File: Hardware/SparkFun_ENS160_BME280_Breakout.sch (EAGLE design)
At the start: 37 parts, among them J1 Qwiic Right Angle, J3 Qwiic Right Angle, J4 PTH, U1 AP2127K-1.8V, U2 ENS-160, U3 BME280

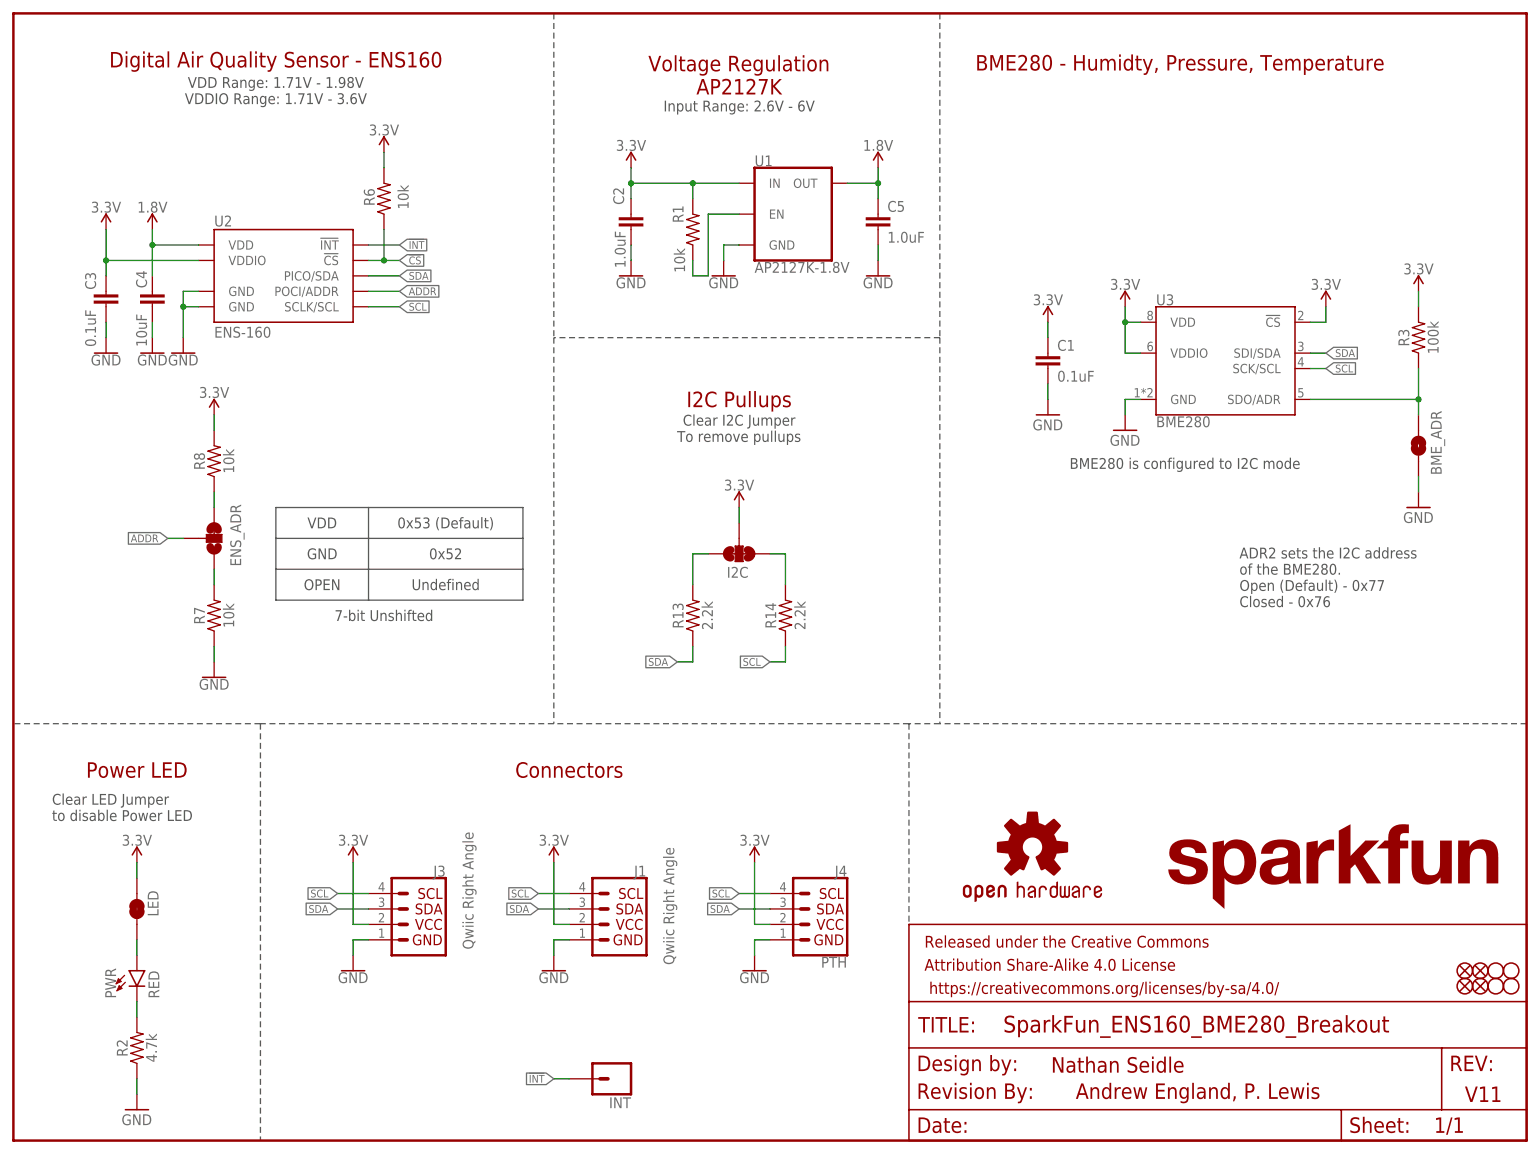
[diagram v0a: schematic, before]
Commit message: added a 100nF cap to VDDIO on BME280
-added C6
-re-routed 3V3 and GND for better return path to GND pads on ICs
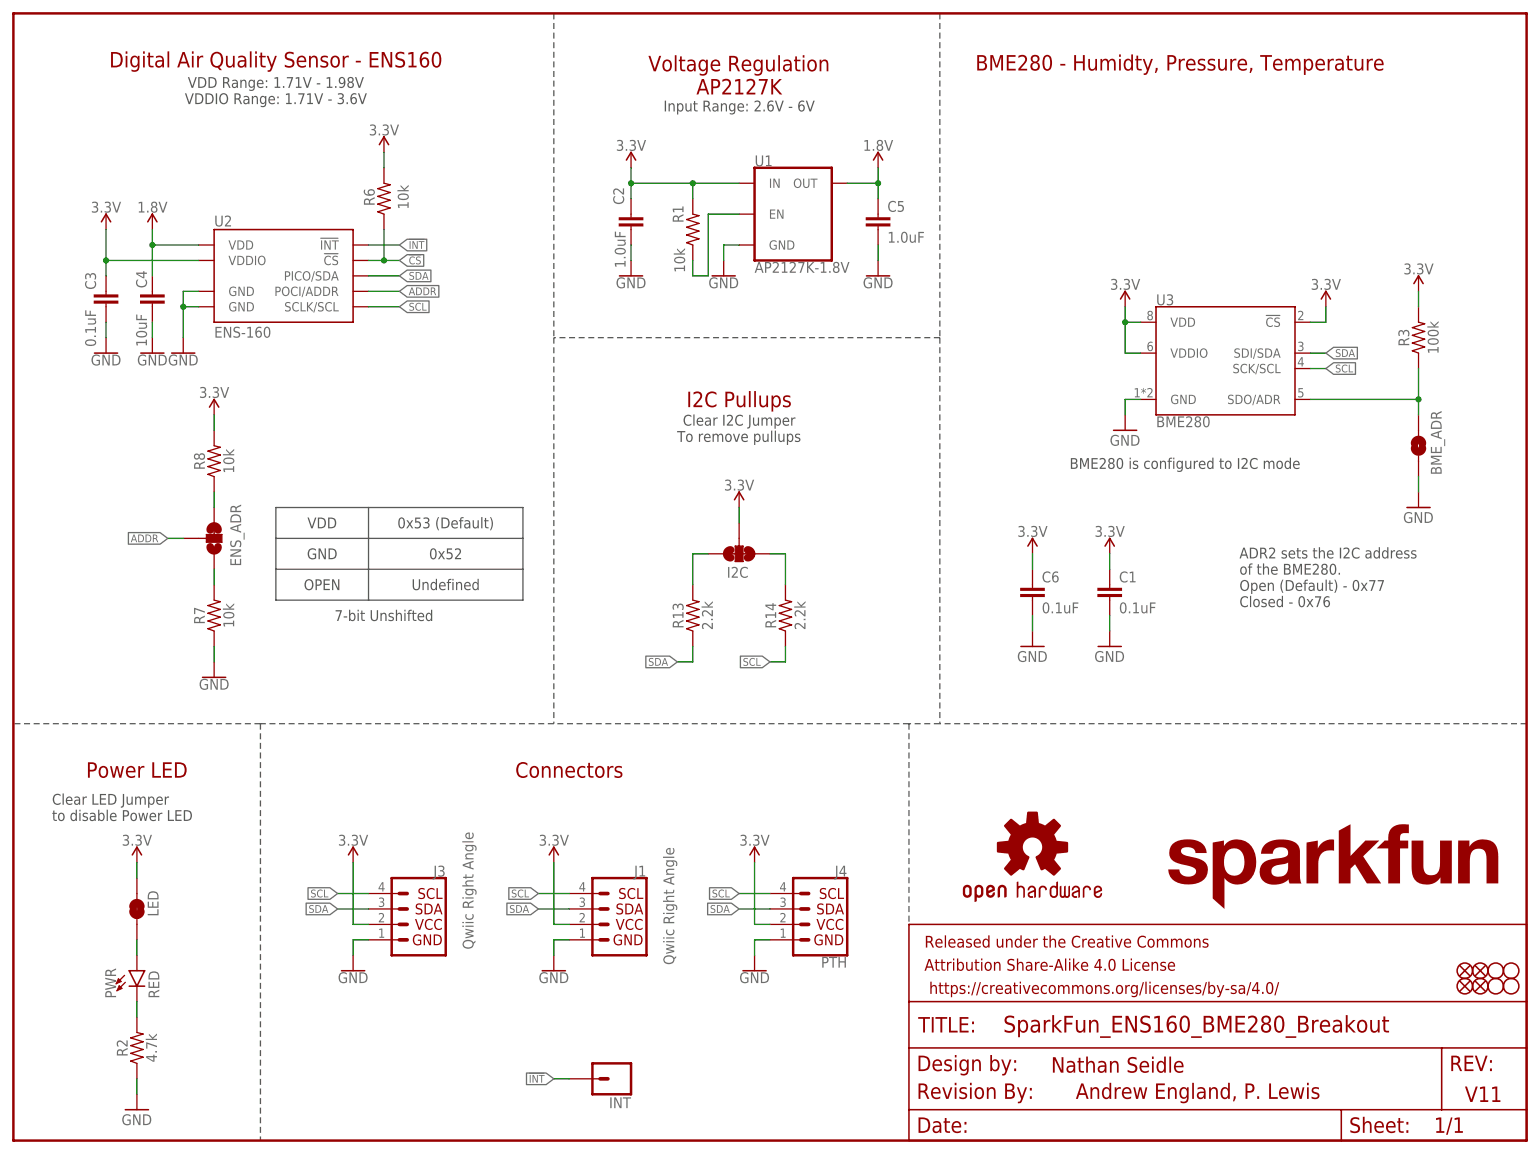
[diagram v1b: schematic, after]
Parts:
- added C6: 0.1uF, SparkFun-Capacitors:0.1UF-0402T-16V-10%
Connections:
- removed net !INT: INT.1
- net !INT!: now also INT.1
- net 3.3V: now also C6.1
- net GND: now also C6.2
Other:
- moved on the sheet: C1
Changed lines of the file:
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@@
 <part name="H1" library="SparkFun-Hardware" deviceset="STAND-OFF" device=""/>
 <part name="H3" library="SparkFun-Hardware" deviceset="STAND-OFF" device=""/>
+<part name="GND13" library="SparkFun-Aesthetics" deviceset="GND" device=""/>
+<part name="C6" library="SparkFun-Capacitors" deviceset="0.1UF" device="-0402T-16V-10%" value="0.1uF"/>
+<part name="SUPPLY13" library="SparkFun-PowerSymbols" deviceset="3.3V" device=""/>
 </parts>
 <sheets>
@@
 <attribute name="VALUE" x="180.34" y="114.3" size="1.778" layer="96" font="vector"/>
 </instance>
-<instance part="GND7" gate="1" x="170.18" y="119.38" smashed="yes">
-<attribute name="VALUE" x="167.64" y="116.84" size="1.778" layer="96" font="vector"/>
-</instance>
-<instance part="C1" gate="G$1" x="170.18" y="127" smashed="yes">
-<attribute name="NAME" x="171.704" y="129.921" size="1.778" layer="95" font="vector"/>
-<attribute name="VALUE" x="171.704" y="124.841" size="1.778" layer="96" font="vector"/>
+<instance part="GND7" gate="1" x="180.34" y="81.28" smashed="yes">
+<attribute name="VALUE" x="177.8" y="78.74" size="1.778" layer="96" font="vector"/>
+</instance>
+<instance part="C1" gate="G$1" x="180.34" y="88.9" smashed="yes">
+<attribute name="NAME" x="181.864" y="91.821" size="1.778" layer="95" font="vector"/>
+<attribute name="VALUE" x="181.864" y="86.741" size="1.778" layer="96" font="vector"/>
 </instance>
 <instance part="GND8" gate="1" x="231.14" y="104.14" smashed="yes">
@@
 <attribute name="VALUE" x="215.9" y="139.954" size="1.778" layer="96" font="vector" align="bottom-center"/>
 </instance>
-<instance part="SUPPLY14" gate="G$1" x="170.18" y="134.62" smashed="yes">
-<attribute name="VALUE" x="170.18" y="137.414" size="1.778" layer="96" font="vector" align="bottom-center"/>
+<instance part="SUPPLY14" gate="G$1" x="180.34" y="96.52" smashed="yes">
+<attribute name="VALUE" x="180.34" y="99.314" size="1.778" layer="96" font="vector" align="bottom-center"/>
 </instance>
 <instance part="U3" gate="U1" x="198.12" y="129.54" smashed="yes">
@@
 <instance part="H1" gate="G$1" x="243.84" y="27.94" smashed="yes"/>
 <instance part="H3" gate="G$1" x="246.38" y="27.94" smashed="yes"/>
+<instance part="GND13" gate="1" x="167.64" y="81.28" smashed="yes">
+<attribute name="VALUE" x="165.1" y="78.74" size="1.778" layer="96" font="vector"/>
+</instance>
+<instance part="C6" gate="G$1" x="167.64" y="88.9" smashed="yes">
+<attribute name="NAME" x="169.164" y="91.821" size="1.778" layer="95" font="vector"/>
+<attribute name="VALUE" x="169.164" y="86.741" size="1.778" layer="96" font="vector"/>
+</instance>
+<instance part="SUPPLY13" gate="G$1" x="167.64" y="96.52" smashed="yes">
+<attribute name="VALUE" x="167.64" y="99.314" size="1.778" layer="96" font="vector" align="bottom-center"/>
+</instance>
 </instances>
 <busses>
@@
 <pinref part="GND7" gate="1" pin="GND"/>
 <pinref part="C1" gate="G$1" pin="2"/>
-<wire x1="170.18" y1="121.92" x2="170.18" y2="124.46" width="0.1524" layer="91"/>
+<wire x1="180.34" y1="83.82" x2="180.34" y2="86.36" width="0.1524" layer="91"/>
 </segment>
 <segment>
@@
 <wire x1="20.32" y1="7.62" x2="20.32" y2="10.16" width="0.1524" layer="91"/>
 </segment>
+<segment>
+<pinref part="GND13" gate="1" pin="GND"/>
+<pinref part="C6" gate="G$1" pin="2"/>
+<wire x1="167.64" y1="83.82" x2="167.64" y2="86.36" width="0.1524" layer="91"/>
+</segment>
 </net>
 <net name="SCL" class="0">
@@
 </segment>
 <segment>
-<wire x1="170.18" y1="132.08" x2="170.18" y2="134.62" width="0.1524" layer="91"/>
+<wire x1="180.34" y1="93.98" x2="180.34" y2="96.52" width="0.1524" layer="91"/>
 <pinref part="C1" gate="G$1" pin="1"/>
 <pinref part="SUPPLY14" gate="G$1" pin="3.3V"/>
@@
 <pinref part="LED" gate="G$1" pin="1"/>
 </segment>
-</net>
-<net name="!INT" class="0">
-<segment>
-<wire x1="91.44" y1="10.16" x2="88.9" y2="10.16" width="0.1524" layer="91"/>
-<label x="88.9" y="10.16" size="1.27" layer="95" font="vector" rot="R180" xref="yes"/>
-<pinref part="INT" gate="J1" pin="1"/>
+<segment>
+<wire x1="167.64" y1="93.98" x2="167.64" y2="96.52" width="0.1524" layer="91"/>
+<pinref part="C6" gate="G$1" pin="1"/>
+<pinref part="SUPPLY13" gate="G$1" pin="3.3V"/>
 </segment>
 </net>
@@
 <label x="63.5" y="147.32" size="1.27" layer="95" font="vector" xref="yes"/>
 </segment>
-</net>
+<segment>
+<label x="88.9" y="10.16" size="1.27" layer="95" font="vector" rot="R180" xref="yes"/>
+<pinref part="INT" gate="J1" pin="1"/>
+<wire x1="88.9" y1="10.16" x2="91.44" y2="10.16" width="0.1524" layer="91"/>
+</segment>
+</net>

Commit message: checklist run eng
-VCC ranges added for bME280
-corrected BME_ADR jumper comment
-moved ENS160 to SFE library
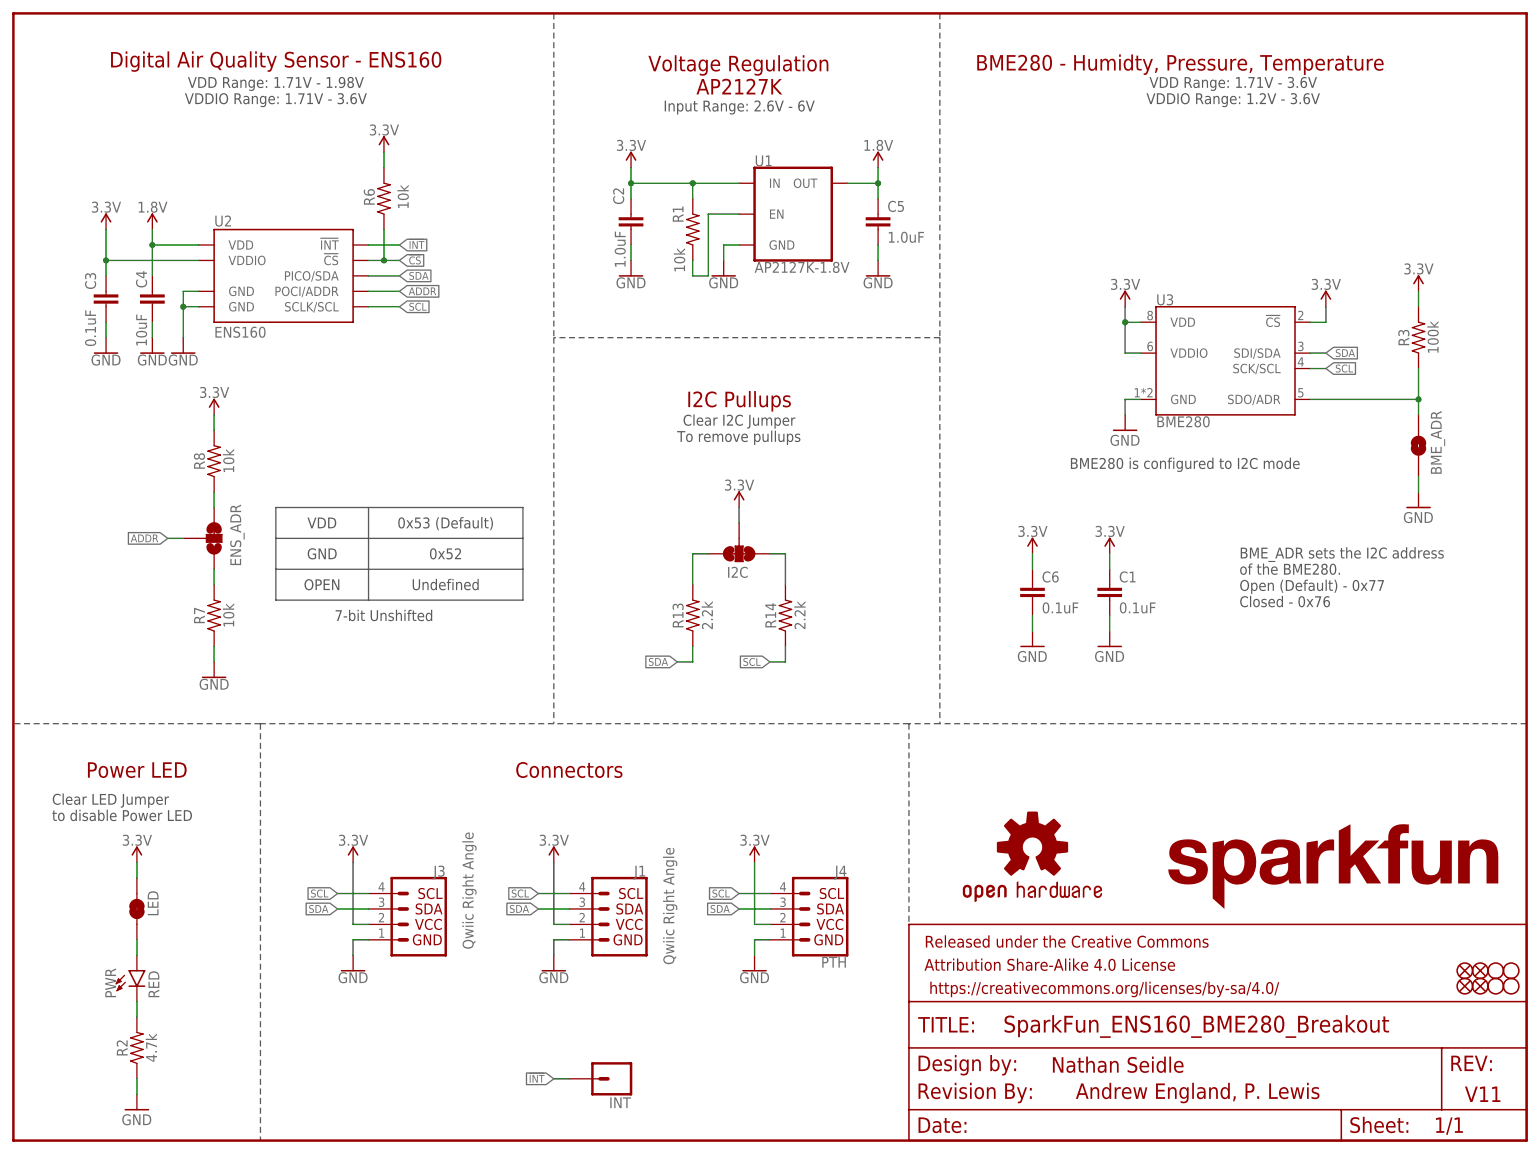
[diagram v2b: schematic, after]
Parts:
- U2: value ENS-160 -> ENS160
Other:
- note added: "BME_ADR sets the I2C address of the BME280. Open (Default) - 0x77 Closed - 0x76"
- note added: "VDD Range: 1.71V - 3.6V VDDIO Range: 1.2V - 3.6V"
- note removed: "ADR2 sets the I2C address of the BME280. Open (Default) - 0x77 Closed - 0x76"
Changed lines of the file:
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@@
 <part name="FD1" library="SparkFun-Aesthetics" deviceset="FIDUCIAL" device="1X2"/>
 <part name="FD2" library="SparkFun-Aesthetics" deviceset="FIDUCIAL" device="1X2"/>
-<part name="GND2" library="SparkFun-Aesthetics" deviceset="GND" device=""/>
-<part name="GND7" library="SparkFun-Aesthetics" deviceset="GND" device=""/>
+<part name="GND2" library="SparkFun-PowerSymbols" deviceset="GND" device=""/>
+<part name="GND7" library="SparkFun-PowerSymbols" deviceset="GND" device=""/>
 <part name="C1" library="SparkFun-Capacitors" deviceset="0.1UF" device="-0402T-16V-10%" value="0.1uF"/>
-<part name="GND8" library="SparkFun-Aesthetics" deviceset="GND" device=""/>
+<part name="GND8" library="SparkFun-PowerSymbols" deviceset="GND" device=""/>
 <part name="R3" library="SparkFun-Resistors" deviceset="100KOHM" device="-0402T-1/16W-1%" value="100k"/>
 <part name="BME_ADR" library="SparkFun-Jumpers" deviceset="JUMPER-SMT_2_NO" device="_SILK" package3d_urn="urn:adsk.eagle:package:39279/1" value=""/>
@@
 <part name="FD3" library="SparkFun-Aesthetics" deviceset="FIDUCIAL" device="1X2"/>
 <part name="FD4" library="SparkFun-Aesthetics" deviceset="FIDUCIAL" device="1X2"/>
-<part name="U2" library="SparkFun-Sensors" deviceset="ENS-160" device=""/>
+<part name="U2" library="SparkFun-Sensors" deviceset="ENS-160" device="" value="ENS160"/>
 <part name="SUPPLY7" library="SparkFun-PowerSymbols" deviceset="1.8V" device=""/>
 <part name="SUPPLY8" library="SparkFun-PowerSymbols" deviceset="3.3V" device=""/>
@@
 <part name="H1" library="SparkFun-Hardware" deviceset="STAND-OFF" device=""/>
 <part name="H3" library="SparkFun-Hardware" deviceset="STAND-OFF" device=""/>
-<part name="GND13" library="SparkFun-Aesthetics" deviceset="GND" device=""/>
+<part name="GND13" library="SparkFun-PowerSymbols" deviceset="GND" device=""/>
 <part name="C6" library="SparkFun-Capacitors" deviceset="0.1UF" device="-0402T-16V-10%" value="0.1uF"/>
 <part name="SUPPLY13" library="SparkFun-PowerSymbols" deviceset="3.3V" device=""/>
@@
 <text x="238.76" y="7.62" size="2.54" layer="94" font="vector" align="center-left">V11</text>
 <text x="170.688" y="12.446" size="2.54" layer="94" font="vector" align="center-left">Nathan Seidle</text>
-<text x="201.676" y="97.536" size="1.778" layer="97" font="vector" align="top-left">ADR2 sets the I2C address
+<text x="201.676" y="97.536" size="1.778" layer="97" font="vector" align="top-left">BME_ADR sets the I2C address
 of the BME280.
 Open (Default) - 0x77
@@
 <text x="91.44" y="60.96" size="2.54" layer="94" font="vector" align="center">Connectors</text>
 <wire x1="147.32" y1="68.58" x2="147.32" y2="35.56" width="0.2032" layer="97" style="longdash"/>
+<text x="200.66" y="172.72" size="1.778" layer="97" font="vector" rot="MR0" align="center">VDD Range: 1.71V - 3.6V
+VDDIO Range: 1.2V - 3.6V</text>
 </plain>
 <instances>
